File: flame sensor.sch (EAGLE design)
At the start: 13 parts, among them T1 BPX81

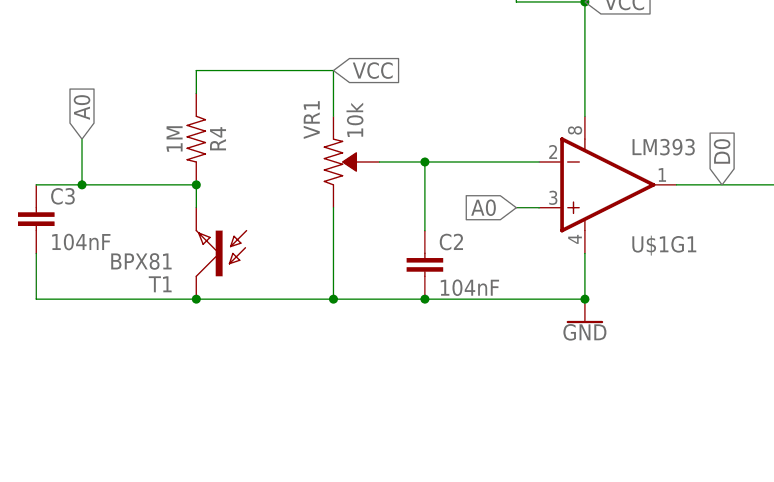
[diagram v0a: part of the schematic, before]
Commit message: changed capacitor
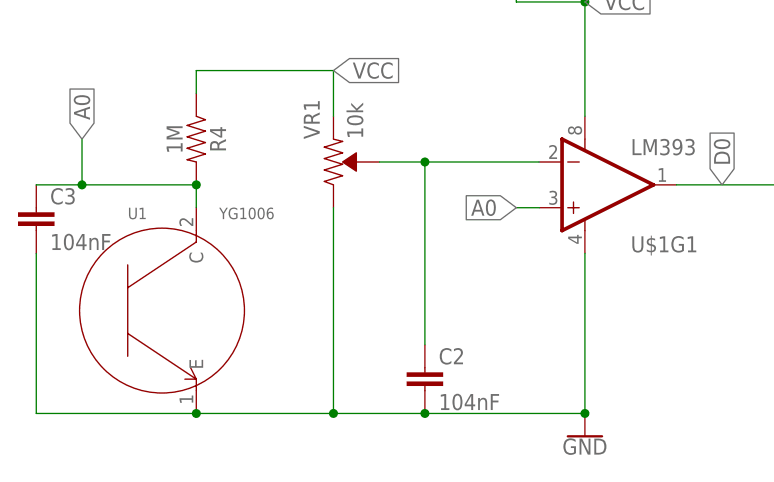
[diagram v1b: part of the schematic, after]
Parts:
- removed T1: BPX81, opto-trans-siemens:BPX81
- added U1: YG1006, template(1):YG1006'YG1006'
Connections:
- net A0: now also U1.C; no longer T1.E
- net GND: now also U1.E; no longer T1.C
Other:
- moved on the sheet: C2
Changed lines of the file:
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@@
 <part name="SUPPLY1" library="SparkFun-PowerSymbols" deviceset="VCC" device=""/>
 <part name="GND1" library="SparkFun-PowerSymbols" deviceset="GND" device=""/>
-<part name="T1" library="opto-trans-siemens" deviceset="BPX81" device=""/>
 <part name="R1" library="SparkFun-Resistors" deviceset="0.05OHM" device="-0603-1/5W-1%" value="1K"/>
 <part name="R2" library="SparkFun-Resistors" deviceset="0.05OHM" device="-0603-1/5W-1%" value="10K"/>
@@
 <part name="VR1" library="SparkFun-Resistors" deviceset="TRIMPOT" device="-SMD-5MM-CLOSED-1/4W-20%" value="10k"/>
 <part name="J1" library="SparkFun-Connectors" deviceset="CONN_04" device=""/>
+<part name="U1" library="template(1)" deviceset="YG1006" device="'YG1006'" value="YG1006"/>
 </parts>
 <sheets>
@@
 <instance part="U$1" gate="G1" x="68.58" y="55.88"/>
 <instance part="SUPPLY1" gate="G$1" x="147.32" y="73.66"/>
-<instance part="GND1" gate="1" x="68.58" y="40.64"/>
-<instance part="T1" gate="1" x="27.94" y="48.26" rot="R180"/>
+<instance part="GND1" gate="1" x="68.58" y="27.94"/>
 <instance part="R1" gate="G$1" x="101.6" y="66.04" rot="R180"/>
 <instance part="R2" gate="G$1" x="101.6" y="55.88" rot="R180"/>
@@
 <instance part="D2" gate="G$1" x="68.58" y="101.6" rot="R180"/>
 <instance part="C1" gate="G$1" x="60.96" y="83.82" rot="R180"/>
-<instance part="C2" gate="G$1" x="50.8" y="45.72"/>
+<instance part="C2" gate="G$1" x="50.8" y="33.02"/>
 <instance part="C3" gate="G$1" x="7.62" y="50.8"/>
 <instance part="VR1" gate="R?" x="40.64" y="58.42"/>
 <instance part="J1" gate="G$1" x="154.94" y="106.68" rot="R180"/>
+<instance part="U1" gate="G$1" x="21.59" y="41.91"/>
 </instances>
 <busses>
@@
 <segment>
 <pinref part="C2" gate="G$1" pin="2"/>
-<wire x1="50.8" y1="43.18" x2="68.58" y2="43.18" width="0.1524" layer="91"/>
+<wire x1="50.8" y1="30.48" x2="68.58" y2="30.48" width="0.1524" layer="91"/>
 <pinref part="VR1" gate="R?" pin="CW"/>
-<wire x1="40.64" y1="53.34" x2="40.64" y2="43.18" width="0.1524" layer="91"/>
-<wire x1="40.64" y1="43.18" x2="50.8" y2="43.18" width="0.1524" layer="91"/>
-<junction x="50.8" y="43.18"/>
-<pinref part="T1" gate="1" pin="C"/>
-<wire x1="25.4" y1="43.18" x2="40.64" y2="43.18" width="0.1524" layer="91"/>
-<junction x="40.64" y="43.18"/>
+<wire x1="40.64" y1="53.34" x2="40.64" y2="30.48" width="0.1524" layer="91"/>
+<wire x1="40.64" y1="30.48" x2="50.8" y2="30.48" width="0.1524" layer="91"/>
+<junction x="50.8" y="30.48"/>
+<junction x="40.64" y="30.48"/>
 <pinref part="C3" gate="G$1" pin="2"/>
-<wire x1="7.62" y1="48.26" x2="7.62" y2="43.18" width="0.1524" layer="91"/>
-<wire x1="7.62" y1="43.18" x2="25.4" y2="43.18" width="0.1524" layer="91"/>
-<junction x="25.4" y="43.18"/>
+<wire x1="7.62" y1="48.26" x2="7.62" y2="30.48" width="0.1524" layer="91"/>
+<wire x1="7.62" y1="30.48" x2="25.4" y2="30.48" width="0.1524" layer="91"/>
 <pinref part="GND1" gate="1" pin="GND"/>
 <pinref part="U$1" gate="G1" pin="V-"/>
-<wire x1="68.58" y1="48.26" x2="68.58" y2="43.18" width="0.1524" layer="91"/>
-<junction x="68.58" y="43.18"/>
+<wire x1="25.4" y1="30.48" x2="40.64" y2="30.48" width="0.1524" layer="91"/>
+<wire x1="68.58" y1="48.26" x2="68.58" y2="30.48" width="0.1524" layer="91"/>
+<junction x="68.58" y="30.48"/>
+<pinref part="U1" gate="G$1" pin="E"/>
+<junction x="25.4" y="30.48"/>
 </segment>
 <segment>
@@
 <wire x1="63.5" y1="58.42" x2="50.8" y2="58.42" width="0.1524" layer="91"/>
 <pinref part="C2" gate="G$1" pin="1"/>
-<wire x1="50.8" y1="58.42" x2="50.8" y2="50.8" width="0.1524" layer="91"/>
+<wire x1="50.8" y1="58.42" x2="50.8" y2="38.1" width="0.1524" layer="91"/>
 <pinref part="VR1" gate="R?" pin="WIPER"/>
 <wire x1="50.8" y1="58.42" x2="45.72" y2="58.42" width="0.1524" layer="91"/>
@@
 <segment>
 <pinref part="R4" gate="G$1" pin="2"/>
-<pinref part="T1" gate="1" pin="E"/>
-<wire x1="25.4" y1="55.88" x2="25.4" y2="53.34" width="0.1524" layer="91"/>
 <pinref part="C3" gate="G$1" pin="1"/>
 <wire x1="25.4" y1="55.88" x2="12.7" y2="55.88" width="0.1524" layer="91"/>
-<junction x="25.4" y="55.88"/>
 <wire x1="12.7" y1="55.88" x2="7.62" y2="55.88" width="0.1524" layer="91"/>
 <wire x1="12.7" y1="55.88" x2="12.7" y2="60.96" width="0.1524" layer="91"/>
 <junction x="12.7" y="55.88"/>
 <label x="12.7" y="60.96" size="1.778" layer="95" rot="R90" xref="yes"/>
+<pinref part="U1" gate="G$1" pin="C"/>
+<wire x1="25.4" y1="55.88" x2="25.4" y2="53.34" width="0.1524" layer="91"/>
+<junction x="25.4" y="55.88"/>
 </segment>
 <segment>
